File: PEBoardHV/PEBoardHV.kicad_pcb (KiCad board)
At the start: 2 copper layers, 106.7 x 76.2 mm, 45 parts, among them J1 To PE LV, J2 Left Connector (Master), J3 E-Meter Internal, J4 Right Connector (Slave), J5 E-Meter External, J6 HV Cable, J7 TSMPs, J8 HV CAN Debug, J9 EMeter HV, U1 L78S05CV-DG, U2 ISO1050, U3 PS2501-4, U4 DK1A1B-12V, U5 DK1A1B-12V

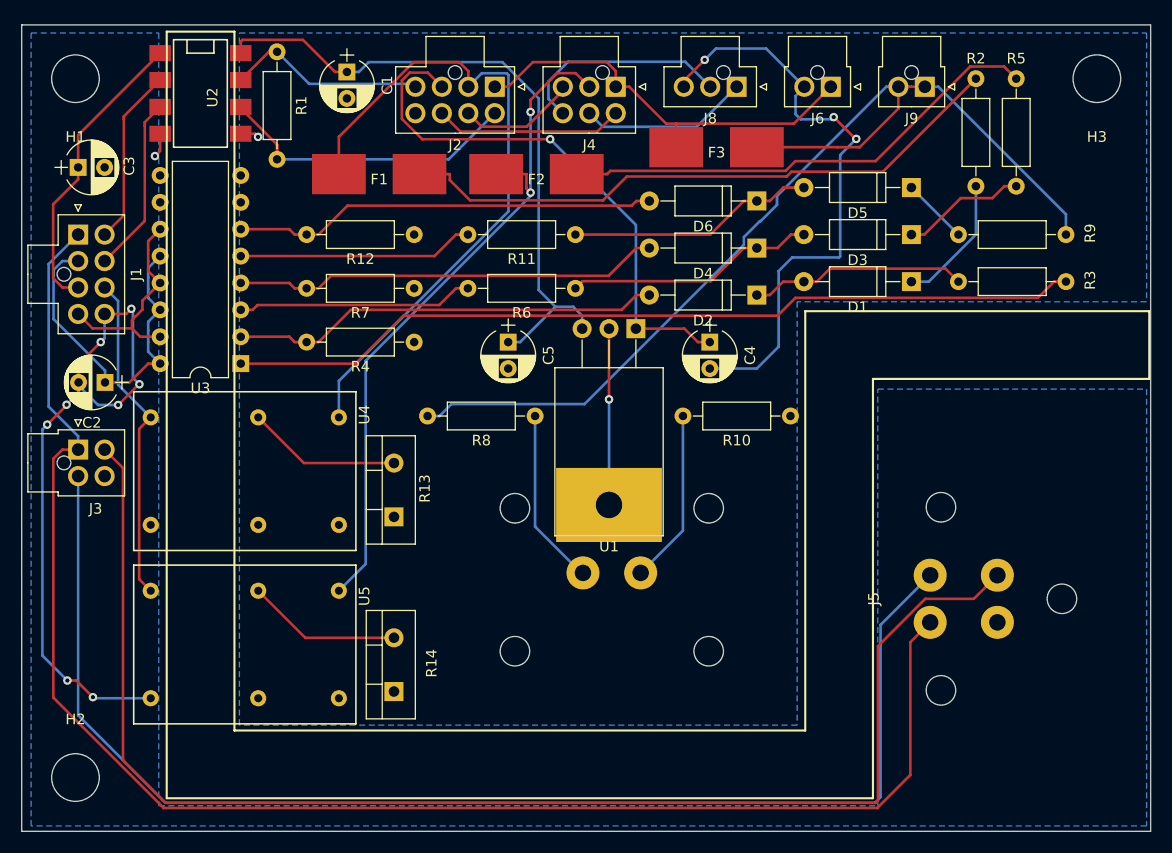
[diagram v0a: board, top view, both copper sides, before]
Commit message: Tweak silkscreen labels on boards for final run
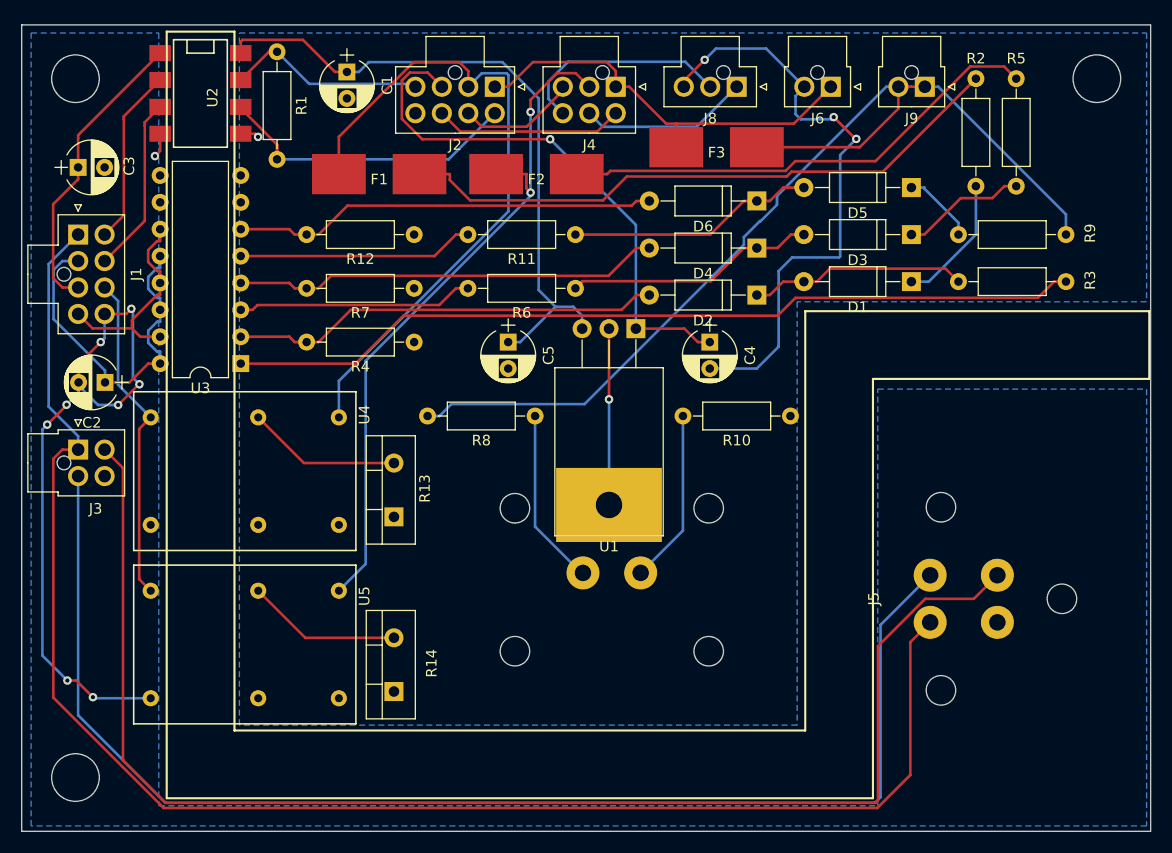
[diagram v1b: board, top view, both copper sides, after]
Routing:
- net Net-(D5-Pad1): track 6.29 -> 7.00 mm
- net /5V_GLV: track 33.3 -> 33.9 mm
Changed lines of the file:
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@@
     (thickness 1.6)
     (drawings 14)
-    (tracks 353)
+    (tracks 362)
     (zones 0)
     (modules 45)
@@
     (tags "mounting hole 4.5mm no annular")
     (attr virtual)
-    (fp_text reference H3 (at 0 -5.5 180) (layer F.SilkS)
+    (fp_text reference H3 (at 0 -5.5 180) (layer F.SilkS) hide
       (effects (font (size 1 1) (thickness 0.15)))
     )
@@
     (tags "mounting hole 4.5mm no annular")
     (attr virtual)
-    (fp_text reference H2 (at 0 -5.5) (layer F.SilkS)
+    (fp_text reference H2 (at 0 -5.5) (layer F.SilkS) hide
       (effects (font (size 1 1) (thickness 0.15)))
     )
@@
     (tags "mounting hole 4.5mm no annular")
     (attr virtual)
-    (fp_text reference H1 (at 0 -5.5 180) (layer F.SilkS)
+    (fp_text reference H1 (at 0 -5.5 180) (layer F.SilkS) hide
       (effects (font (size 1 1) (thickness 0.15)))
     )
@@
   (gr_line (start 140.5 117.983) (end 194.437 117.983) (angle 90) (layer F.SilkS) (width 0.2))
   (gr_line (start 140.5 51.943) (end 140.5 117.983) (angle 90) (layer F.SilkS) (width 0.2))
-  (segment (start 132.3517 75.184) (end 132.3517 74.2773) (width 0.25) (layer B.Cu) (net 1))
-  (segment (start 132.3517 74.2773) (end 133.477 73.152) (width 0.25) (layer B.Cu) (net 1) (status 800000))
-  (segment (start 132.3517 76.2628) (end 132.3517 77.1067) (width 0.25) (layer B.Cu) (net 1))
-  (segment (start 132.3517 77.1067) (end 133.477 78.232) (width 0.25) (layer B.Cu) (net 1) (status 800000))
-  (segment (start 132.3517 80.2012) (end 132.3517 79.3573) (width 0.25) (layer B.Cu) (net 1))
-  (segment (start 132.3517 79.3573) (end 133.477 78.232) (width 0.25) (layer B.Cu) (net 1) (status 800000))
-  (segment (start 132.3517 81.28) (end 132.3517 82.1867) (width 0.25) (layer B.Cu) (net 1))
-  (segment (start 132.3517 82.1867) (end 133.477 83.312) (width 0.25) (layer B.Cu) (net 1) (status 800000))
-  (segment (start 132.3517 81.28) (end 132.3517 80.2012) (width 0.25) (layer B.Cu) (net 1))
   (segment (start 123.4092 79.1039) (end 128.27 83.9647) (width 0.25) (layer B.Cu) (net 1))
   (segment (start 123.4092 74.4594) (end 123.4092 79.1039) (width 0.25) (layer B.Cu) (net 1))
@@
   (segment (start 128.27 85.09) (end 128.27 83.9647) (width 0.25) (layer B.Cu) (net 1))
   (segment (start 130.5737 85.09) (end 132.3517 83.312) (width 0.25) (layer F.Cu) (net 1))
+  (segment (start 128.27 85.09) (end 130.5737 85.09) (width 0.25) (layer F.Cu) (net 1))
   (segment (start 133.477 83.312) (end 132.3517 83.312) (width 0.25) (layer F.Cu) (net 1))
-  (segment (start 128.27 85.09) (end 130.5737 85.09) (width 0.25) (layer F.Cu) (net 1))
-  (segment (start 132.3517 76.2628) (end 132.3517 75.184) (width 0.25) (layer B.Cu) (net 1))
+  (segment (start 133.1956 74.2773) (end 133.477 74.2773) (width 0.25) (layer B.Cu) (net 1))
+  (segment (start 132.3517 75.1212) (end 133.1956 74.2773) (width 0.25) (layer B.Cu) (net 1))
+  (segment (start 132.3517 76.2628) (end 132.3517 75.1212) (width 0.25) (layer B.Cu) (net 1))
+  (segment (start 133.1956 77.1067) (end 132.3517 76.2628) (width 0.25) (layer B.Cu) (net 1))
+  (segment (start 133.477 77.1067) (end 133.1956 77.1067) (width 0.25) (layer B.Cu) (net 1))
+  (segment (start 133.477 73.152) (end 133.477 74.2773) (width 0.25) (layer B.Cu) (net 1))
+  (segment (start 133.477 78.232) (end 133.477 77.1067) (width 0.25) (layer B.Cu) (net 1))
+  (segment (start 133.1956 79.3573) (end 133.477 79.3573) (width 0.25) (layer B.Cu) (net 1))
+  (segment (start 132.3517 80.2012) (end 133.1956 79.3573) (width 0.25) (layer B.Cu) (net 1))
+  (segment (start 132.3517 81.3427) (end 132.3517 80.2012) (width 0.25) (layer B.Cu) (net 1))
+  (segment (start 133.1957 82.1867) (end 132.3517 81.3427) (width 0.25) (layer B.Cu) (net 1))
+  (segment (start 133.477 82.1867) (end 133.1957 82.1867) (width 0.25) (layer B.Cu) (net 1))
+  (segment (start 133.477 83.312) (end 133.477 82.1867) (width 0.25) (layer B.Cu) (net 1))
+  (segment (start 133.477 78.232) (end 133.477 79.3573) (width 0.25) (layer B.Cu) (net 1))
   (segment (start 125.77 85.09) (end 125.77 85.384) (width 0.25) (layer B.Cu) (net 2))
   (segment (start 125.77 85.384) (end 127.6096 87.2236) (width 0.25) (layer B.Cu) (net 2))
@@
   (segment (start 175.8495 75.0202) (end 149.625 75.0202) (width 0.25) (layer F.Cu) (net 12))
   (segment (start 178.4797 72.39) (end 175.8495 75.0202) (width 0.25) (layer F.Cu) (net 12))
-  (segment (start 204.47 66.675) (end 208.915 71.12) (width 0.25) (layer B.Cu) (net 13))
+  (segment (start 205.6953 66.775) (end 208.915 69.9947) (width 0.25) (layer B.Cu) (net 13))
+  (segment (start 205.6953 66.675) (end 205.6953 66.775) (width 0.25) (layer B.Cu) (net 13))
+  (segment (start 204.47 66.675) (end 205.6953 66.675) (width 0.25) (layer B.Cu) (net 13))
+  (segment (start 208.915 71.12) (end 208.915 69.9947) (width 0.25) (layer B.Cu) (net 13))
   (segment (start 185.4647 71.12) (end 172.72 71.12) (width 0.25) (layer F.Cu) (net 14))
   (segment (start 188.6397 67.945) (end 185.4647 71.12) (width 0.25) (layer F.Cu) (net 14))
@@
   (segment (start 124.2429 91.44) (end 123.3841 92.2988) (width 0.25) (layer F.Cu) (net 22))
   (segment (start 125.73 91.44) (end 124.2429 91.44) (width 0.25) (layer F.Cu) (net 22))
-  (segment (start 131.8035 78.2095) (end 131.8035 77.3655) (width 0.25) (layer F.Cu) (net 23))
-  (segment (start 131.8035 77.3655) (end 133.477 75.692) (width 0.25) (layer F.Cu) (net 23))
-  (segment (start 132.3517 73.66) (end 132.3517 74.5667) (width 0.25) (layer F.Cu) (net 23))
-  (segment (start 132.3517 73.66) (end 132.3517 72.5812) (width 0.25) (layer F.Cu) (net 23))
-  (segment (start 132.3517 71.7373) (end 133.477 70.612) (width 0.25) (layer F.Cu) (net 23))
-  (segment (start 132.3517 72.5812) (end 132.3517 71.7373) (width 0.25) (layer F.Cu) (net 23))
-  (segment (start 132.3517 74.5667) (end 133.477 75.692) (width 0.25) (layer F.Cu) (net 23))
   (segment (start 133.477 80.772) (end 132.3517 80.772) (width 0.25) (layer F.Cu) (net 23))
+  (segment (start 133.1956 71.7373) (end 133.477 71.7373) (width 0.25) (layer F.Cu) (net 23))
+  (segment (start 132.3517 72.5812) (end 133.1956 71.7373) (width 0.25) (layer F.Cu) (net 23))
+  (segment (start 132.3517 73.7227) (end 132.3517 72.5812) (width 0.25) (layer F.Cu) (net 23))
+  (segment (start 133.1957 74.5667) (end 132.3517 73.7227) (width 0.25) (layer F.Cu) (net 23))
+  (segment (start 133.477 74.5667) (end 133.1957 74.5667) (width 0.25) (layer F.Cu) (net 23))
+  (segment (start 133.477 75.692) (end 133.477 74.5667) (width 0.25) (layer F.Cu) (net 23))
+  (segment (start 133.477 70.612) (end 133.477 71.7373) (width 0.25) (layer F.Cu) (net 23))
+  (segment (start 133.477 75.692) (end 133.477 76.8173) (width 0.25) (layer F.Cu) (net 23))
   (segment (start 127.0945 79.9845) (end 125.73 78.62) (width 0.25) (layer F.Cu) (net 23))
   (segment (start 130.8159 79.9845) (end 127.0945 79.9845) (width 0.25) (layer F.Cu) (net 23))
   (segment (start 131.6034 80.772) (end 130.8159 79.9845) (width 0.25) (layer F.Cu) (net 23))
   (segment (start 132.3517 80.772) (end 131.6034 80.772) (width 0.25) (layer F.Cu) (net 23))
-  (segment (start 130.8159 79.1971) (end 131.8035 78.2095) (width 0.25) (layer F.Cu) (net 23))
+  (segment (start 133.1957 76.8173) (end 133.477 76.8173) (width 0.25) (layer F.Cu) (net 23))
+  (segment (start 130.8159 79.1971) (end 133.1957 76.8173) (width 0.25) (layer F.Cu) (net 23))
   (segment (start 130.8159 79.9845) (end 130.8159 79.1971) (width 0.25) (layer F.Cu) (net 23))
   (segment (start 132.0244 60.7794) (end 132.0244 60.5076) (width 0.25) (layer F.Cu) (net 24))

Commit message: Revise boards based on design review
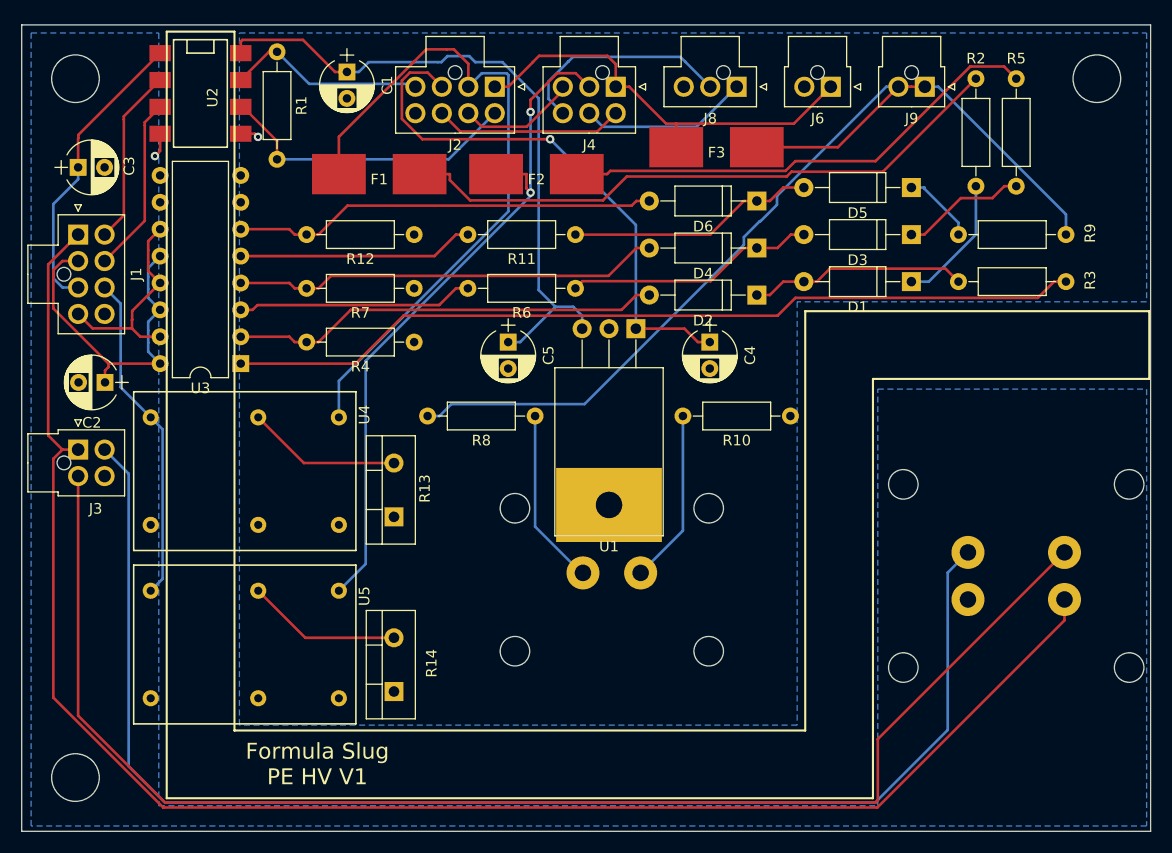
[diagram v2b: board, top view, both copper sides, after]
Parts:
- J5: footprint FSFootprints:DT13-4P -> FSFootprints:DT15-4P; moved to B.Cu
- moved J5 4.83 mm to (214.4, 103.4)
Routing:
- net /TS-: track 75.6 -> 1.76 mm, vias 5 -> 1
- net GND: track 66.7 -> 2.31 mm, vias 9 -> 1
- net /EM_SIG+: track 125.0 -> 132.4 mm
- net +12V: track 149.7 -> 156.5 mm
- net /EM_SIG-: track 131.8 -> 130.1 mm
- net /5V_GLV: track 33.9 -> 32.5 mm
- net /TS+_SWITCHED_L: track 63.9 -> 65.3 mm
- net /CAN_L_BOARD: track 30.1 -> 28.9 mm
- net /TS+_FUSED: track 98.0 -> 96.8 mm
- net /TS+: track 39.7 -> 40.5 mm
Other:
- board text added: "Formula Slug PE HV V1"

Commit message: Change TSMP resistors
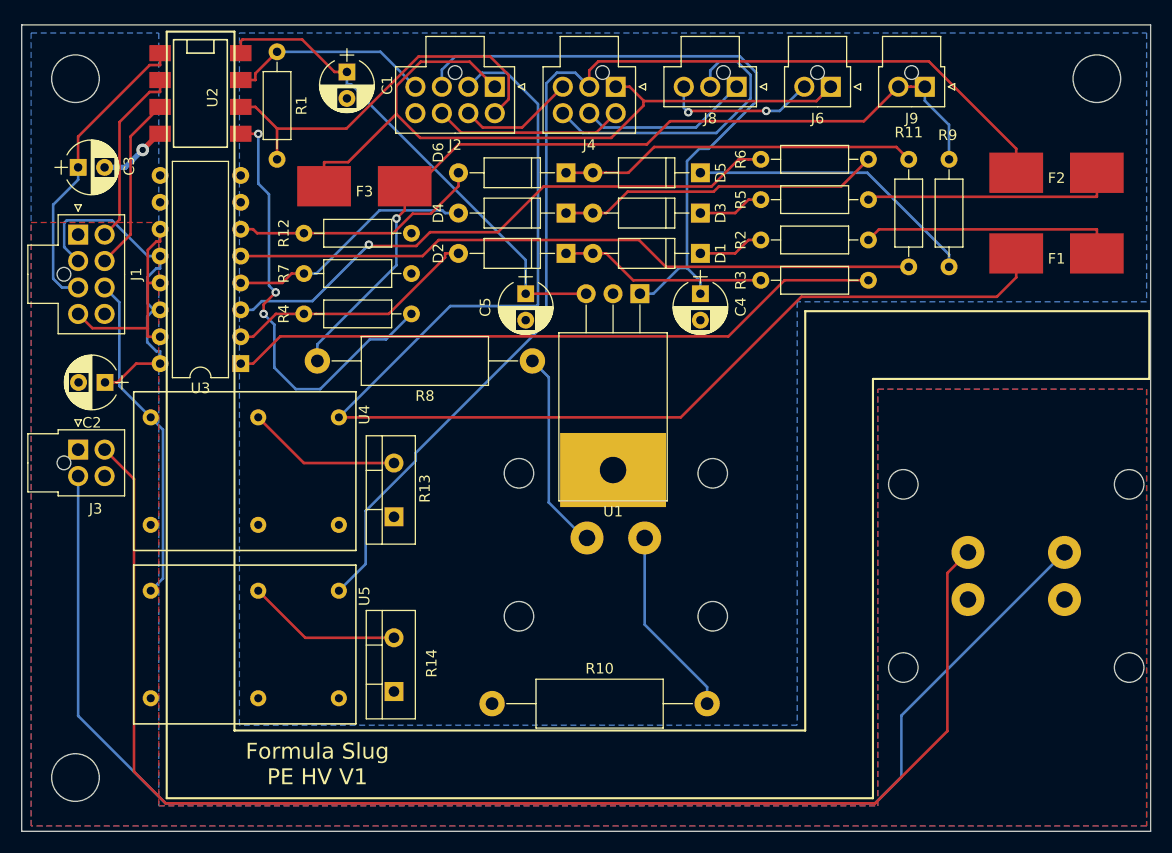
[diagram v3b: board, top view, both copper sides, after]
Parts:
- R10, R8: footprint Resistors_THT:R_Axial_DIN0207_L6.3mm_D2.5mm_P10.16mm_Horizontal -> Resistors_THT:R_Axial_DIN0414_L11.9mm_D4.5mm_P20.32mm_Horizontal
- moved F1 64.4 mm to (218.2, 72.9)
- moved F2 49.1 mm to (218.2, 65.3)
- moved R10 39.2 mm to (164.8, 115.4), turned to 0 degrees
- moved F3 33.5 mm to (152.8, 66.5)
- moved R11 32.3 mm to (204.2, 64.0), turned to 270 degrees
- moved R6 30.3 mm to (200.4, 64.0)
- moved D1 20.1 mm to (184.5, 72.9)
- moved D3 20.0 mm to (184.5, 69.1)
- moved D5 20.0 mm to (184.5, 65.3)
- moved R3 18.7 mm to (190.2, 75.4)
- moved D2 18.5 mm to (171.8, 72.9)
- moved D4 18.3 mm to (171.8, 69.1)
- moved R2 18.3 mm to (200.4, 71.6), turned to 180 degrees
- moved D6 18.2 mm to (171.8, 65.3)
- moved R5 18.1 mm to (200.4, 67.8), turned to 180 degrees
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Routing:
- net +12V: track 156.5 -> 0.00 mm
- net /TS+_SWITCHED_L: track 65.3 -> 122.3 mm
- net /TS-: track 1.76 -> 56.6 mm, vias 1 -> 5
- net /TS+_SWITCHED_R: track 65.8 -> 109.0 mm, vias 2 -> 0
- net Net-(R11-Pad2): track 22.3 -> 64.8 mm
- net Net-(F1-Pad2): track 58.7 -> 24.3 mm
- net Net-(R6-Pad2): track 22.3 -> 55.1 mm, vias 0 -> 1
- net /TS+: track 40.5 -> 72.3 mm
- net Net-(F2-Pad2): track 46.2 -> 24.0 mm
- net Net-(D5-Pad1): track 7.00 -> 27.9 mm
- net Net-(R3-Pad2): track 81.2 -> 62.6 mm
- net Net-(D4-Pad2): track 40.4 -> 23.5 mm
- net /5V_TS: track 63.1 -> 46.4 mm
- net Net-(D2-Pad2): track 40.7 -> 24.1 mm
- net Net-(D6-Pad2): track 40.1 -> 23.8 mm
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- added copper zone on F.Cu, net +12V
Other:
- net class Default: clearance 0.2 -> 0.24
- net class EMPower added: clearance 0.24, trace_width 0.5, via_dia 1.2, via_drill 0.6
- rule trace_clearance: 0.2 -> 0.24

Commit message: Un-fuse TSMPs
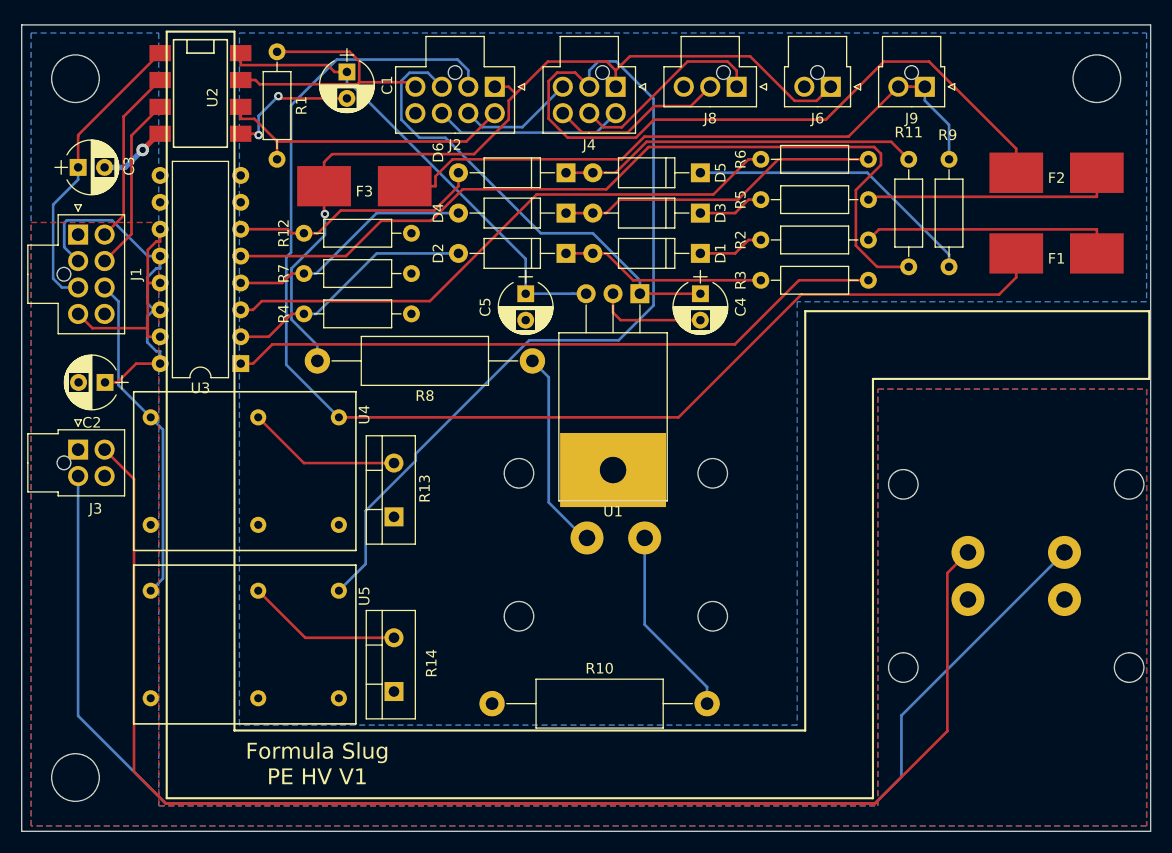
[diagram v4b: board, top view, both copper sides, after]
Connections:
- R8 pad 2: /TS+_FUSED -> /TS+
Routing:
- net /TS-: track 56.6 -> 23.1 mm, vias 5 -> 2
- net /TS+_SWITCHED_R: track 109.0 -> 135.0 mm
- net /TS+_FUSED: track 81.2 -> 61.4 mm, vias 1 -> 0
- net /CAN+: track 62.6 -> 44.2 mm
- net Net-(R11-Pad2): track 64.8 -> 80.5 mm
- net /CAN_L_DEBUG: track 28.3 -> 16.5 mm
- net /TS+: track 72.3 -> 81.0 mm, vias 0 -> 1
- net /CAN_L_BOARD: track 36.8 -> 28.8 mm
- net /CAN_H_BOARD: track 19.3 -> 27.0 mm
- net /CAN_H_DEBUG: track 16.1 -> 18.9 mm
- net /TS+_SWITCHED_L: track 122.3 -> 124.0 mm
- net /5V_TS: track 46.4 -> 45.3 mm
- net /3.3V_GLV: track 28.8 -> 28.2 mm
- net /CAN_RX: track 17.4 -> 16.8 mm
- net Net-(R6-Pad2): track 55.1 -> 55.0 mm, vias 1 -> 0
